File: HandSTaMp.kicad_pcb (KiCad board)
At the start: 2 copper layers, 40.6 x 16.5 mm, 25 parts, among them J1 USB_C_Receptacle_USB2.0_16P, J2 SWD, J3 Pins, J4 F2, SW0 BOOT, SW1 Row 0, Col+0, SW2 Row 0, Col+1, U1 STM32C071GBUx, U2 PRTR5V0U2X, U3 XC6206P332MR-G

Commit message: Draft of version using CH32X035G8U6
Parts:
- removed C1, C2: 1µF, Capacitor_SMD:C_0603_1608Metric
- removed C5: 100nF, Capacitor_SMD:C_0603_1608Metric
- removed J4: F2, TestPoint:TestPoint_THTPad_D1.0mm_Drill0.5mm
- removed R4: 10kΩ, Resistor_SMD:R_0603_1608Metric
- removed R5: 330Ω, Resistor_SMD:R_0603_1608Metric
- removed U1: STM32C071GBUx, Package_DFN_QFN:QFN-28_4x4mm_P0.5mm
- removed U3: XC6206P332MR-G, Package_TO_SOT_SMD:SOT-23-3
- added U4: CH32X035G8U6, Package_DFN_QFN:WQFN-28-1EP_4x4mm_P0.4mm_EP2.7x2.7mm, F.Cu at (102.2, 55.2)
- R3: value 5k1Ω -> 5.k1Ω
- moved R3 27.1 mm to (88.2, 50.8), turned to 90 degrees
- moved J2 17.8 mm to (107.7, 52.1), turned to -90 degrees
- moved C3 3.10 mm to (96.8, 53.9)
- moved C4 3.10 mm to (98.3, 53.9)
- moved SW0 2.16 mm to (92.1, 54.5)
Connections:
- C3 pad 1: +3V3 -> VCC
- C4 pad 1: +3V3 -> VCC
- J2 pad 2: BOOT0/SWCLK -> SWCLK
- J3 pad 2: +3V3 -> VCC
- R3 pad 1: RGB -> Net-(R3-Pad1)
- SW0 pad 1: BOOT0/SWCLK -> USB+
- SW0 pad 2: Net-(R5-Pad1) -> Net-(R3-Pad1)
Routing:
- net +3V3: track 28.1 -> 0.00 mm, vias 3 -> 0
- net BOOT0/SWCLK: track 22.0 -> 0.00 mm
- net C1: track 18.8 -> 35.6 mm
- net GND: track 16.6 -> 4.23 mm, vias 19 -> 11
- net USB+: track 9.89 -> 19.6 mm
- net VCC: track 48.2 -> 57.3 mm, vias 3 -> 6
- net SWDIO: track 12.1 -> 3.96 mm
- net R0: track 52.3 -> 58.5 mm, vias 5 -> 2
- net NRST: track 4.88 -> 0.00 mm, vias 1 -> 0
- net SWCLK: track 0.00 -> 4.70 mm
- net Net-(R3-Pad1): track 0.00 -> 4.48 mm
- net PC14: track 11.5 -> 8.41 mm
- net ISLAND: track 0.00 -> 2.93 mm
- net Net-(R5-Pad1): track 2.56 -> 0.00 mm
- net C0: track 27.0 -> 25.1 mm
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- removed copper zone on F.Cu, net GND

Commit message: Tweak routing and silkscreen, and update README
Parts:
- renumbered C3 to C1, C4 to C2
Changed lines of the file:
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@@
 		)
 		(property "Label" "3"
-			(at 0.025401 0 270)
+			(at 0 0.0254 90)
 			(unlocked yes)
 			(layer "F.SilkS")
@@
 		)
 		(embedded_fonts no)
-		(model "${KICAD10_3DMODEL_DIR}/Package_DFN_QFN.3dshapes/WQFN-28-1EP_4x4mm_P0.4mm_EP2.7x2.7mm.step"
+		(model "${KICAD10_3DMODEL_DIR}/Package_DFN_QFN.3dshapes/UQFN-28-1EP_4x4mm_P0.4mm_EP2.35x2.35mm.step"
 			(offset
 				(xyz 0 0 0)
@@
 		(tags "fuse")
 		(property "Reference" "F1"
-			(at 0 -1.016 90)
+			(at 0 -1.143 90)
 			(layer "F.SilkS")
+			(hide yes)
 			(effects
 				(font
@@
 			)
 		)
+		(property "Label" "F"
+			(at 0 -0.0254 90)
+			(unlocked yes)
+			(layer "F.SilkS")
+			(effects
+				(font
+					(size 0.6 0.6)
+					(thickness 0.1)
+				)
+			)
+		)
 		(property ki_fp_filters "*polyfuse* *PTC*")
 		(sheetname "/")
@@
 		(descr "Capacitor SMD 0603 (1608 Metric), square (rectangular) end terminal, IPC-7351 nominal, (Body size source: IPC-SM-782 page 76, https://www.pcb-3d.com/wordpress/wp-content/uploads/ipc-sm-782a_amendment_1_and_2.pdf)")
 		(tags "capacitor")
-		(property "Reference" "C4"
+		(property "Reference" "C2"
 			(at 1.778 0 0)
 			(layer "F.SilkS")
@@
 		)
 		(property "Value" "100nF"
-			(at 0.0635 1.016 270)
+			(at -1.222305 0 90)
 			(unlocked yes)
 			(layer "F.SilkS")
+			(hide yes)
 			(effects
 				(font
@@
 					(thickness 0.1)
 				)
+				(justify right)
 			)
 		)
@@
 			)
 		)
+		(property "Label" "n"
+			(at 0 -0.075 90)
+			(unlocked yes)
+			(layer "F.SilkS")
+			(effects
+				(font
+					(size 0.6 0.6)
+					(thickness 0.1)
+				)
+			)
+		)
 		(property ki_fp_filters "C_*")
 		(sheetname "/")
@@
 		(descr "Capacitor SMD 0603 (1608 Metric), square (rectangular) end terminal, IPC-7351 nominal, (Body size source: IPC-SM-782 page 76, https://www.pcb-3d.com/wordpress/wp-content/uploads/ipc-sm-782a_amendment_1_and_2.pdf)")
 		(tags "capacitor")
-		(property "Reference" "C3"
+		(property "Reference" "C1"
 			(at 1.778 0 0)
 			(layer "F.SilkS")
@@
 		)
 		(property "Value" "4µ7F"
-			(at 0.0635 -1.397 90)
+			(at -1.222305 0 270)
 			(layer "F.SilkS")
+			(hide yes)
 			(effects
 				(font
@@
 					(thickness 0.1)
 				)
+				(justify right)
 			)
 		)
@@
 			)
 		)
+		(property "Label" "µ"
+			(at 0 -0.175 90)
+			(unlocked yes)
+			(layer "F.SilkS")
+			(effects
+				(font
+					(size 0.6 0.6)
+					(thickness 0.1)
+				)
+			)
+		)
 		(property ki_fp_filters "C_*")
 		(sheetname "/")
@@
 	)
 	(segment
-		(start 114.935 50.70475)
-		(end 114.935 48.26)
+		(start 112.649 53.467)
+		(end 114.935 51.181)
 		(width 0.1524)
 		(layer "F.Cu")
@@
 	)
 	(segment
-		(start 112.649 52.99075)
-		(end 114.935 50.70475)
+		(start 103.634384 53.254195)
+		(end 103.802579 53.086)
 		(width 0.1524)
 		(layer "F.Cu")
@@
 	)
 	(segment
-		(start 103.441195 53.213)
-		(end 105.918 53.213)
+		(start 105.841052 53.467)
+		(end 112.649 53.467)
 		(width 0.1524)
 		(layer "F.Cu")
@@
 	)
 	(segment
-		(start 112.649 53.467)
-		(end 112.649 52.99075)
+		(start 105.460052 53.086)
+		(end 105.841052 53.467)
 		(width 0.1524)
 		(layer "F.Cu")
@@
 	(segment
 		(start 103.4 53.254195)
-		(end 103.441195 53.213)
+		(end 103.634384 53.254195)
 		(width 0.1524)
 		(layer "F.Cu")
@@
 	)
 	(segment
-		(start 114.554 56.134)
-		(end 118.11 59.69)
+		(start 103.802579 53.086)
+		(end 105.460052 53.086)
 		(width 0.1524)
 		(layer "F.Cu")
@@
 	)
 	(segment
-		(start 106.172 53.467)
-		(end 112.649 53.467)
+		(start 114.554 56.134)
+		(end 118.11 59.69)
 		(width 0.1524)
 		(layer "F.Cu")
@@
 	)
 	(segment
-		(start 105.918 53.213)
-		(end 106.172 53.467)
+		(start 114.935 51.181)
+		(end 114.935 48.26)
 		(width 0.1524)
 		(layer "F.Cu")
@@
 	)
 	(segment
-		(start 84.455 53.213)
-		(end 87.63 56.388)
+		(start 85.344 50.165)
+		(end 85.344 47.2117)
 		(width 0.1524)
 		(layer "F.Cu")
@@
 	)
 	(segment
-		(start 105.9434 54.0004)
-		(end 113.032863 54.0004)
+		(start 84.455 51.054)
+		(end 85.344 50.165)
 		(width 0.1524)
 		(layer "F.Cu")
@@
 	)
 	(segment
-		(start 85.344 47.2117)
-		(end 85.344 50.165)
+		(start 94.7166 53.153668)
+		(end 94.7166 56.0324)
 		(width 0.1524)
 		(layer "F.Cu")
@@
 	)
 	(segment
-		(start 104.606305 54.016695)
-		(end 104.902 53.721)
+		(start 98.905485 51.9938)
+		(end 95.876468 51.9938)
 		(width 0.1524)
 		(layer "F.Cu")
@@
 	)
 	(segment
-		(start 105.664 53.721)
-		(end 105.9434 54.0004)
+		(start 104.775 53.6575)
+		(end 105.6005 53.6575)
 		(width 0.1524)
 		(layer "F.Cu")
@@
 	)
 	(segment
-		(start 94.361 56.388)
-		(end 94.7166 56.0324)
+		(start 95.876468 51.9938)
+		(end 94.7166 53.153668)
 		(width 0.1524)
 		(layer "F.Cu")
@@
 	)
 	(segment
-		(start 104.902 53.721)
-		(end 105.283 53.721)
+		(start 87.63 56.388)
+		(end 84.455 53.213)
 		(width 0.1524)
 		(layer "F.Cu")
@@
 	)
 	(segment
-		(start 95.876468 51.9938)
-		(end 98.905485 51.9938)
+		(start 113.032863 54.0004)
+		(end 117.856 49.177263)
 		(width 0.1524)
 		(layer "F.Cu")
@@
 	)
 	(segment
-		(start 117.856 47.2117)
-		(end 120.65 44.45)
+		(start 100.457 52.705)
+		(end 99.616685 52.705)
 		(width 0.1524)
 		(layer "F.Cu")
@@
 	)
 	(segment
-		(start 84.455 51.054)
-		(end 84.455 53.213)
+		(start 104.3305 53.6575)
+		(end 104.775 53.6575)
 		(width 0.1524)
 		(layer "F.Cu")
@@
 	)
 	(segment
-		(start 105.283 53.721)
-		(end 105.664 53.721)
+		(start 94.7166 56.0324)
+		(end 94.361 56.388)
 		(width 0.1524)
 		(layer "F.Cu")
@@
 	)
 	(segment
-		(start 98.905485 51.9938)
-		(end 99.91188 53.000195)
+		(start 117.856 47.2117)
+		(end 120.65 44.45)
 		(width 0.1524)
 		(layer "F.Cu")
@@
 	)
 	(segment
-		(start 94.7166 53.153668)
-		(end 95.876468 51.9938)
+		(start 104.1625 54.016695)
+		(end 104.1625 53.8255)
 		(width 0.1524)
 		(layer "F.Cu")
@@
 	)
 	(segment
-		(start 113.032863 54.0004)
-		(end 117.856 49.177263)
+		(start 94.361 56.388)
+		(end 87.63 56.388)
 		(width 0.1524)
 		(layer "F.Cu")
@@
 	)
 	(segment
-		(start 94.7166 56.0324)
-		(end 94.7166 53.153668)
+		(start 105.9434 54.0004)
+		(end 113.032863 54.0004)
 		(width 0.1524)
 		(layer "F.Cu")
@@
 	)
 	(segment
-		(start 104.1625 54.016695)
-		(end 104.606305 54.016695)
+		(start 84.455 53.213)
+		(end 84.455 51.054)
 		(width 0.1524)
 		(layer "F.Cu")
@@
 	)
 	(segment
-		(start 99.91188 53.000195)
-		(end 100.33 53.000195)
+		(start 104.1625 53.8255)
+		(end 104.3305 53.6575)
 		(width 0.1524)
 		(layer "F.Cu")
@@
 	)
 	(segment
-		(start 82.55 44.45)
-		(end 85.344 47.2117)
+		(start 105.6005 53.6575)
+		(end 105.9434 54.0004)
 		(width 0.1524)
 		(layer "F.Cu")
@@
 	)
 	(segment
-		(start 87.63 56.388)
-		(end 94.361 56.388)
+		(start 82.55 44.45)
+		(end 85.344 47.2117)
 		(width 0.1524)
 		(layer "F.Cu")
@@
 	)
 	(segment
-		(start 85.344 50.165)
-		(end 84.455 51.054)
+		(start 117.856 49.177263)
+		(end 117.856 47.2117)
 		(width 0.1524)
 		(layer "F.Cu")
@@
 	)
 	(segment
-		(start 117.856 49.177263)
-		(end 117.856 47.2117)
+		(start 99.616685 52.705)
+		(end 98.905485 51.9938)
 		(width 0.1524)
 		(layer "F.Cu")
@@
 	)
 	(via
-		(at 100.33 53.000195)
+		(at 100.457 52.705)
 		(size 0.508)
 		(drill 0.254)
@@
 	)
 	(via
-		(at 105.283 53.721)
+		(at 104.775 53.6575)
 		(size 0.508)
 		(drill 0.254)
@@
 	)
 	(segment
-		(start 105.156 53.721)
-		(end 105.283 53.848)
+		(start 100.457 53.127195)
+		(end 100.457 52.705)
 		(width 0.1524)
 		(layer "B.Cu")
@@
 	)
 	(segment
-		(start 100.33 53.000195)
-		(end 101.050805 53.721)
+		(start 104.775 53.6575)
+		(end 100.987305 53.6575)
 		(width 0.1524)
 		(layer "B.Cu")
@@
 	)
 	(segment
-		(start 101.050805 53.721)
-		(end 105.156 53.721)
+		(start 100.987305 53.6575)
+		(end 100.457 53.127195)
 		(width 0.1524)
 		(layer "B.Cu")

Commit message: Further routing tweaks
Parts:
- moved SW0 2.03 mm to (90.0, 54.5)
- moved R3 0.13 mm to (88.3, 50.8)
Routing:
- net GND: track 4.23 -> 8.76 mm, vias 11 -> 13
- net Net-(R3-Pad1): track 4.48 -> 2.89 mm
- net PA15: track 26.4 -> 27.5 mm
- net R0: track 58.4 -> 59.2 mm

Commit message: Update internal and external pin labelling
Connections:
- net PA15 renamed PC15
- net PA5 renamed PB1
- net RGB renamed PB9
- J3 pad 10: PB7 -> PA2
- J3 pad 11: PB8 -> PA3
- J3 pad 12: PC14 -> PA4
- J3 pad 14: PA0 -> PA6
- J3 pad 15: PA1 -> PA7
- J3 pad 16: PA2 -> PB0
- J3 pad 17: PA3 -> PB3
- J3 pad 18: PA4 -> PB4
- J3 pad 20: PA6 -> PB6
- J3 pad 22: PB0 -> PB8
- J3 pad 23: PA7 -> PB7
- J3 pad 6: PB3 -> PC0
- J3 pad 7: PB4 -> PC3
- J3 pad 8: PB5 -> PA0
- J3 pad 9: PB6 -> PA1
- U4 pad 11: PA0 -> PA6
- U4 pad 12: PA1 -> PA7
- U4 pad 13: PA2 -> PB0
- U4 pad 14: PA3 -> PB3
- U4 pad 15: PA4 -> PB4
- U4 pad 17: PA6 -> PB6
- U4 pad 18: PA7 -> PB7
- U4 pad 19: PB0 -> PB8
- U4 pad 3: PB3 -> PC0
- U4 pad 4: PB4 -> PC3
- U4 pad 5: PB5 -> PA0
- U4 pad 6: PB6 -> PA1
- U4 pad 7: PB7 -> PA2
- U4 pad 8: PB8 -> PA3
- U4 pad 9: PC14 -> PA4
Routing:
- net PC0: track 0.00 -> 19.6 mm
- net PC3: track 0.00 -> 19.5 mm
- net PB5: track 16.8 -> 0.00 mm
- net PA0: track 4.91 -> 16.8 mm
- net PA7: track 17.5 -> 6.74 mm
- net PA6: track 14.9 -> 4.91 mm
- net PB3: track 19.6 -> 10.8 mm
- net PC14: track 8.41 -> 0.00 mm
- net PA1: track 6.74 -> 14.1 mm
- net PB4: track 19.5 -> 12.8 mm
- net PB7: track 11.4 -> 17.5 mm
- net PB0: track 14.0 -> 8.81 mm
- net PA4: track 12.8 -> 8.41 mm
- net PB8: track 10.0 -> 14.0 mm
- net PA2: track 8.81 -> 11.4 mm
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
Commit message: Fix pin 16
This can PB1 or PB5, but the latter is the default.
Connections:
- net PB1 renamed PB5
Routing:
- net USB+: track 19.5 -> 21.4 mm

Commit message: Update SWD/SDI and Shield connections
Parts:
- added J4: ⏚, Project Library:SolderWire_1x01_D1mm_OD1.7mm, F.Cu at (92.1, 43.8)
- J2: value SWD -> SDI; footprint Project Library:SWD+GroundingPoint -> Project Library:SWD
- moved J2 1.27 mm to (106.4, 52.1), turned to 180 degrees
- renumbered SW0 to S3
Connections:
- J2 pad 1: ISLAND -> SWCLK
- J2 pad 2: SWCLK -> SWDIO
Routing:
- net ISLAND: track 2.93 -> 0.00 mm
- net SWDIO: track 3.96 -> 5.16 mm

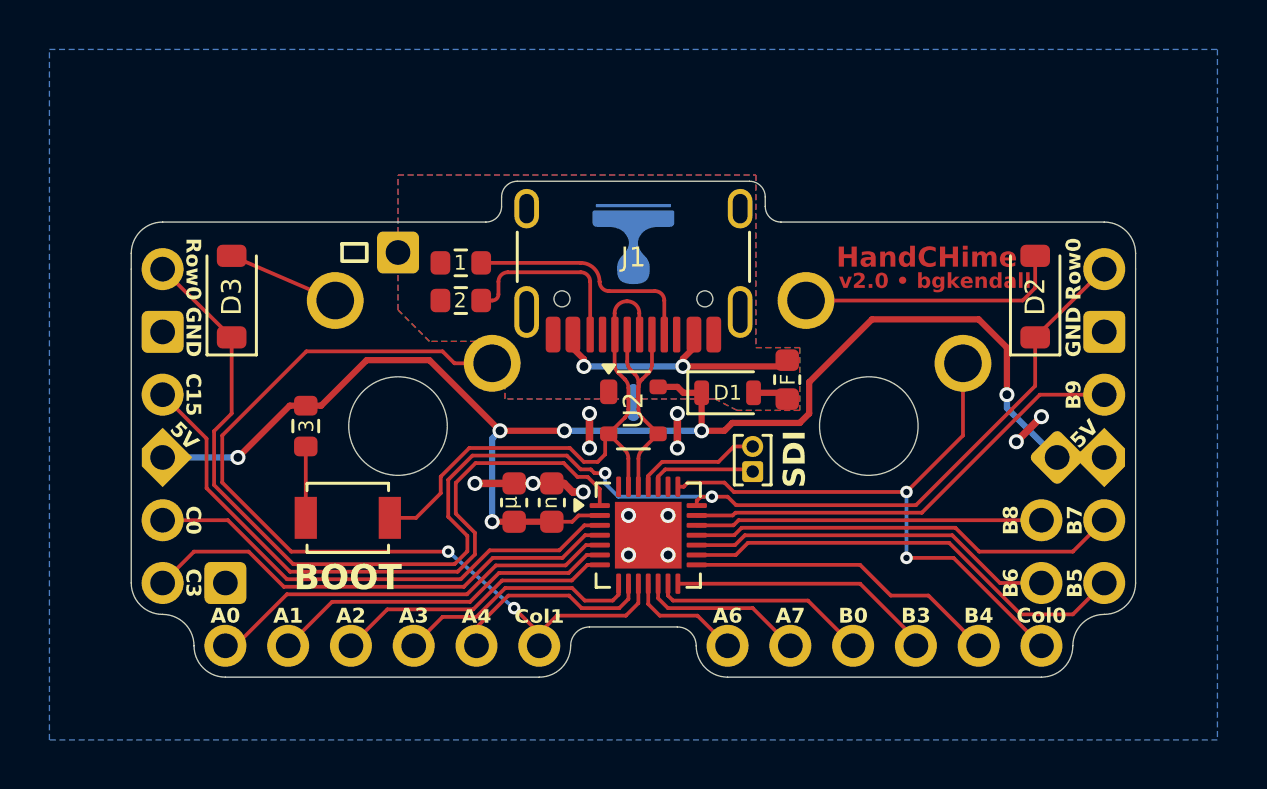
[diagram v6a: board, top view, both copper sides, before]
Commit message: Add one alignment pin hole to each MX switch
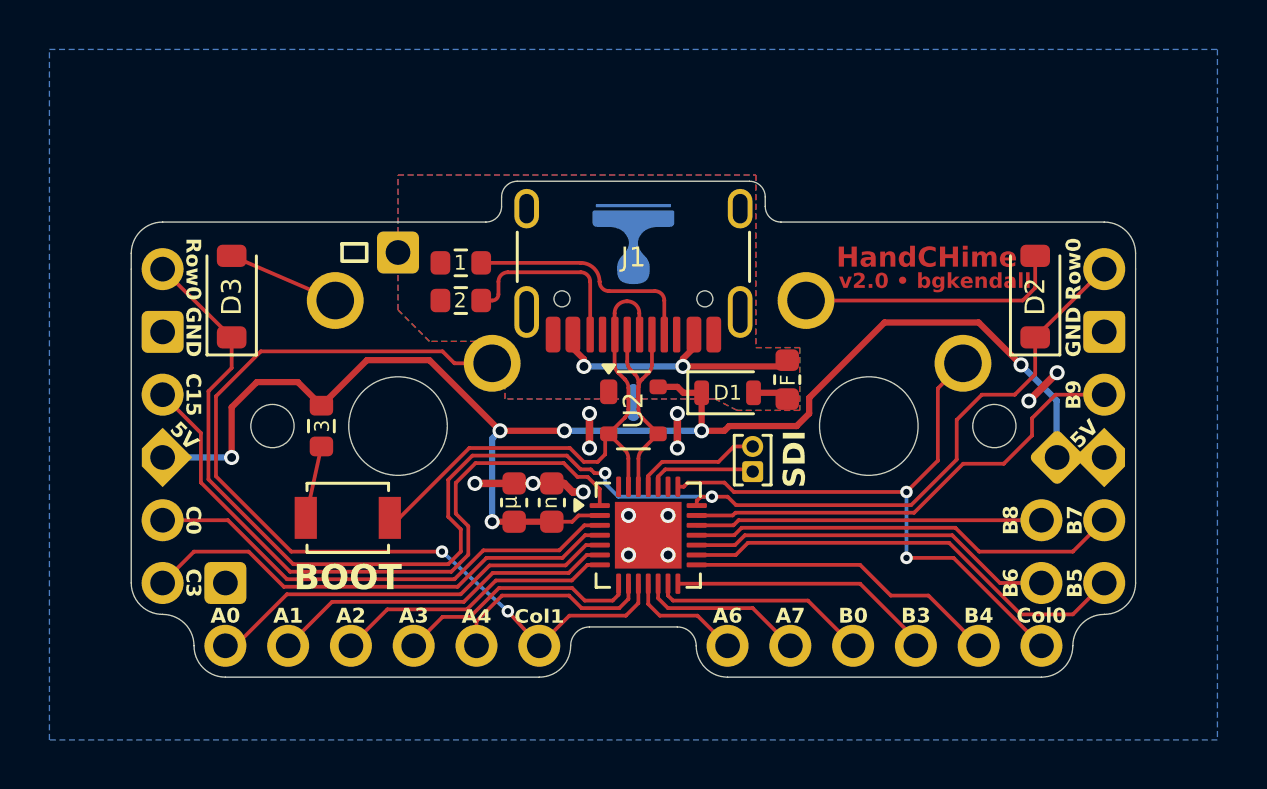
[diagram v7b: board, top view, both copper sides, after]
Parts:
- SW1: footprint Project Library:SW_MX_1u_PlateMount -> Project Library:SW_MX_1u_1pinL
- SW2: footprint Project Library:SW_MX_1u_PlateMount -> Project Library:SW_MX_1u_1pinR
- moved R3 0.63 mm to (89.0, 50.8)
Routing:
- net C1: track 35.6 -> 37.1 mm
- net VCC: track 57.4 -> 58.5 mm
